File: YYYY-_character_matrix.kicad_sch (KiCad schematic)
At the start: 17 parts, among them U1 SN74LVC244A, U2 SM411006N/15, U3 SM411006N/15, U4 SN74LVC244A, U5 SM411006N/15, U6 SM411006N/15, U7 SM411006N/15

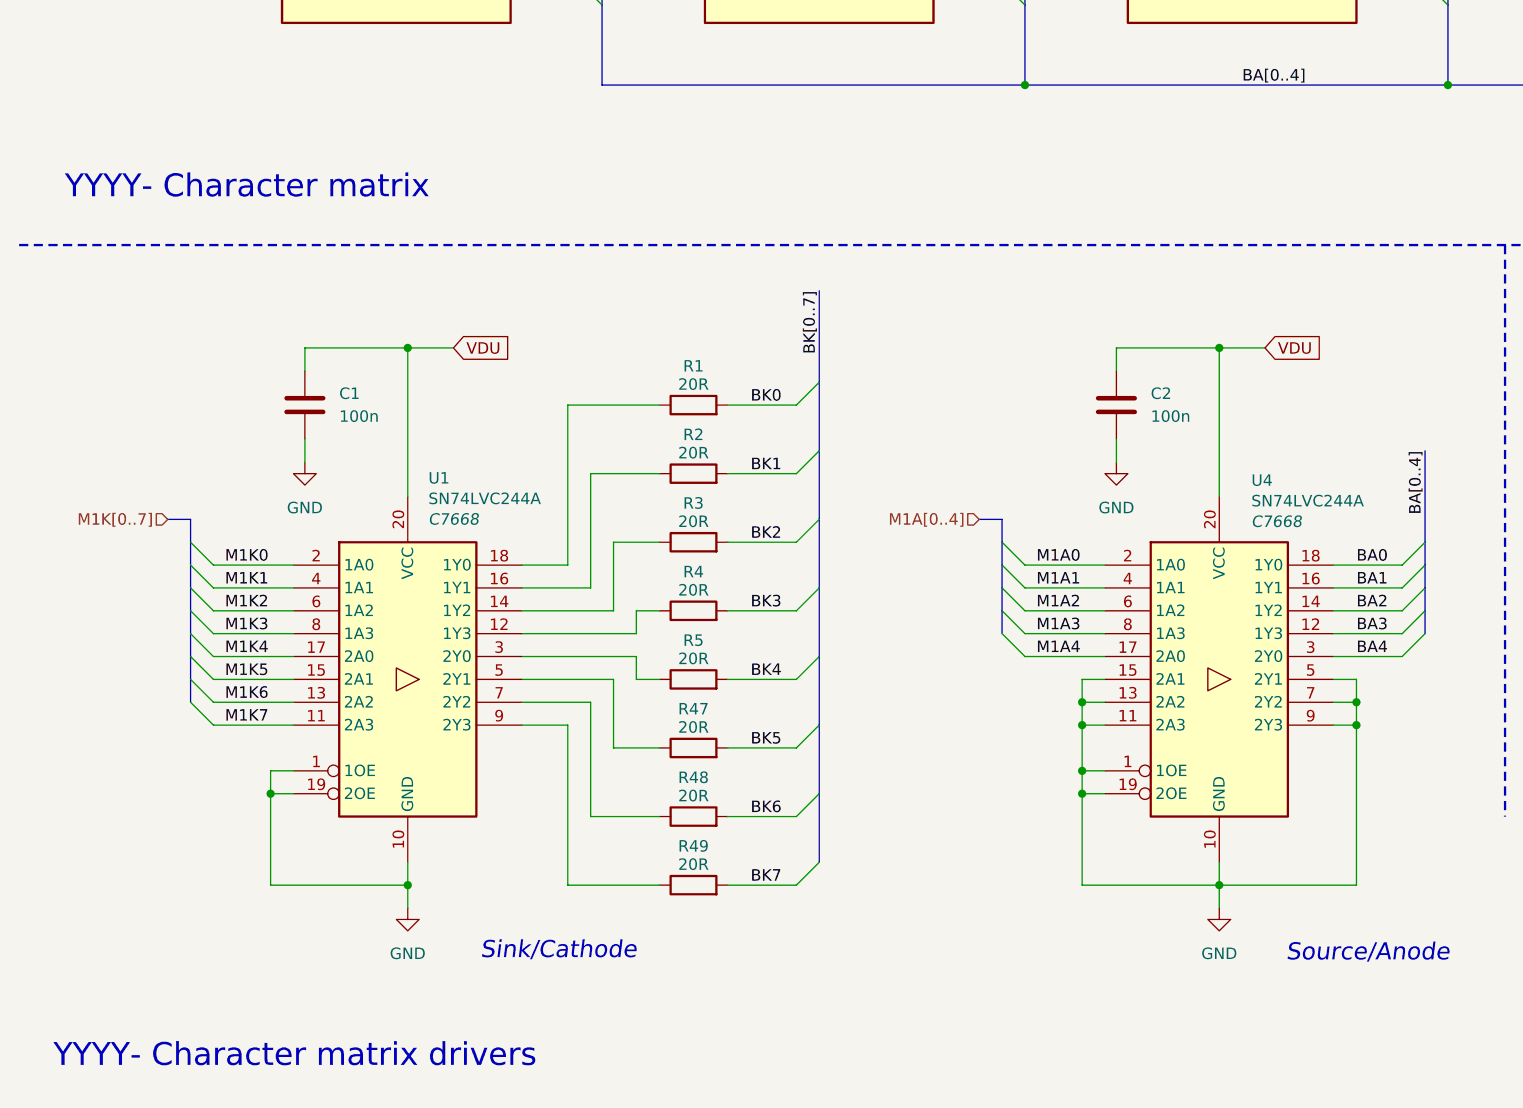
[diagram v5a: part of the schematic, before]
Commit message: verification
- sensor schematic verification
- change in the value of current limiting resistor
- disconnected unused buffer pins
- labeling or peripherals used in primary MCU
- additional user button
- DRC corrections
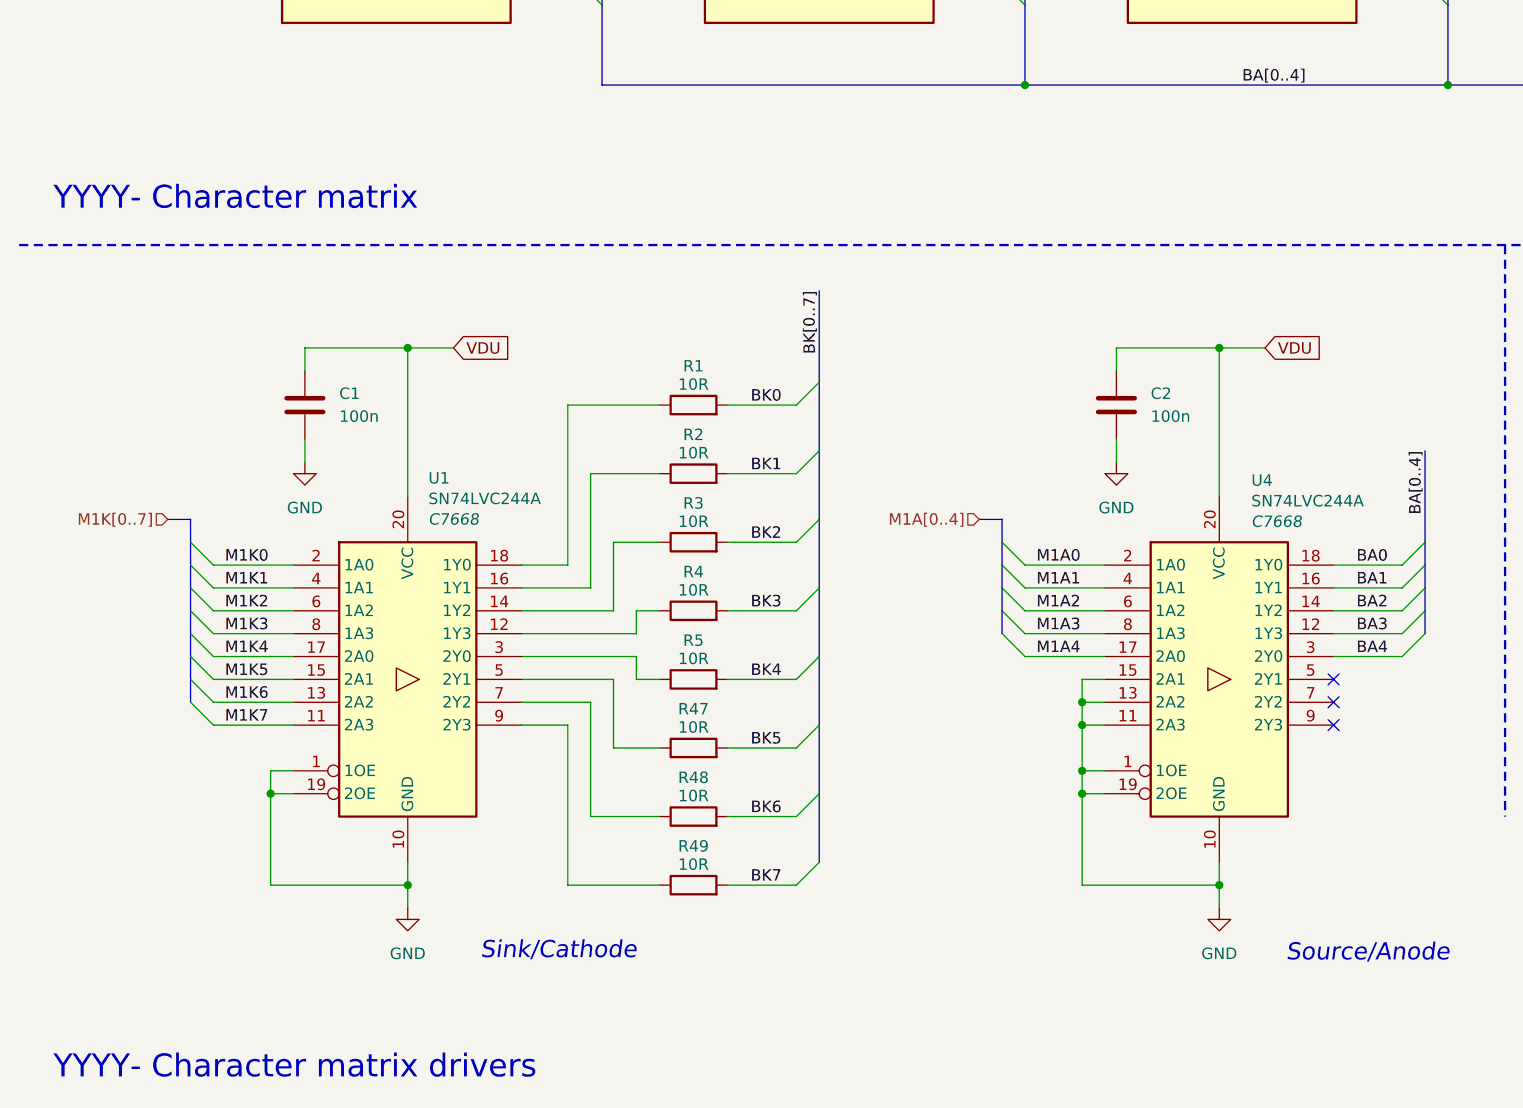
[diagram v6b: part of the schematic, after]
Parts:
- R1, R2, R3, R4, R47, R48, R49, R5: value 20R -> 10R
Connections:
- net GND: no longer U4.5 (2Y1), U4.7 (2Y2), U4.9 (2Y3)
- no-connect marks 0 -> 3
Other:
- company: Rajath Katker -> TJ71PL
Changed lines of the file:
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@@
 	(title_block
 		(title "YYYY- Character Matrix & Drivers ")
-		(date "2025-11-04")
+		(date "2025-09-05")
 		(rev "v0.0")
-		(company "Rajath Katker")
+		(company "TJ71PL")
+		(comment 1 "天計")
 		(comment 4 "Final verification pending")
 	)
@@
 	(text "YYYY- Character matrix"
 		(exclude_from_sim no)
-		(at 17.78 95.25 0)
+		(at 16.51 96.52 0)
 		(effects
 			(font
@@
 	(text "YYYY- Character matrix drivers "
 		(exclude_from_sim no)
-		(at 16.51 191.77 0)
+		(at 16.51 193.04 0)
 		(effects
 			(font
@@
 	)
 	(junction
-		(at 161.29 152.4)
-		(diameter 0)
-		(color 0 0 0 0)
-	)
-	(junction
 		(at 130.81 160.02)
 		(diameter 0)
@@
 	)
 	(junction
-		(at 161.29 154.94)
-		(diameter 0)
-		(color 0 0 0 0)
-	)
-	(junction
 		(at 78.74 31.75)
 		(diameter 0)
@@
 		(color 0 0 0 0)
 	)
+	(no_connect
+		(at 158.75 149.86)
+	)
+	(no_connect
+		(at 158.75 152.4)
+	)
+	(no_connect
+		(at 158.75 154.94)
+	)
 	(bus_entry
 		(at 31.75 142.24)
@@
 		)
 	)
-	(wire
-		(pts
-			(xy 158.75 149.86) (xy 161.29 149.86)
-		)
-		(stroke
-			(width 0)
-			(type default)
-		)
-	)
 	(bus
 		(pts
@@
 	(wire
 		(pts
-			(xy 161.29 149.86) (xy 161.29 152.4)
-		)
-		(stroke
-			(width 0)
-			(type default)
-		)
-	)
-	(wire
-		(pts
 			(xy 163.83 69.85) (xy 168.91 69.85)
 		)
@@
 		)
 	)
-	(wire
-		(pts
-			(xy 158.75 154.94) (xy 161.29 154.94)
-		)
-		(stroke
-			(width 0)
-			(type default)
-		)
-	)
 	(bus
 		(pts
@@
 	(wire
 		(pts
-			(xy 161.29 172.72) (xy 146.05 172.72)
-		)
-		(stroke
-			(width 0)
-			(type default)
-		)
-	)
-	(wire
-		(pts
 			(xy 91.44 149.86) (xy 99.06 149.86)
 		)
@@
 	(wire
 		(pts
-			(xy 161.29 154.94) (xy 161.29 172.72)
-		)
-		(stroke
-			(width 0)
-			(type default)
-		)
-	)
-	(wire
-		(pts
 			(xy 222.25 62.23) (xy 227.33 62.23)
 		)
@@
 		)
 	)
-	(wire
-		(pts
-			(xy 161.29 152.4) (xy 161.29 154.94)
-		)
-		(stroke
-			(width 0)
-			(type default)
-		)
-	)
 	(bus
 		(pts
@@
 	(wire
 		(pts
-			(xy 158.75 152.4) (xy 161.29 152.4)
-		)
-		(stroke
-			(width 0)
-			(type default)
-		)
-	)
-	(wire
-		(pts
 			(xy 146.05 172.72) (xy 146.05 175.26)
 		)
@@
 			)
 		)
-		(property "Value" "20R"
+		(property "Value" "10R"
 			(at 87.63 117.094 90)
 			(effects
@@
 			)
 		)
-		(property "Value" "20R"
+		(property "Value" "10R"
 			(at 87.63 132.334 90)
 			(effects
@@
 			)
 		)
-		(property "Value" "20R"
+		(property "Value" "10R"
 			(at 87.63 139.954 90)
 			(effects
@@
 			)
 		)
-		(property "Value" "20R"
+		(property "Value" "10R"
 			(at 87.63 155.194 90)
 			(effects
@@
 			)
 		)
-		(property "Value" "20R"
+		(property "Value" "10R"
 			(at 87.63 162.814 90)
 			(effects
@@
 			)
 		)
-		(property "Value" "20R"
+		(property "Value" "10R"
 			(at 87.63 124.714 90)
 			(effects
@@
 			)
 		)
-		(property "Value" "20R"
+		(property "Value" "10R"
 			(at 87.63 147.574 90)
 			(effects
@@
 			)
 		)
-		(property "Value" "20R"
+		(property "Value" "10R"
 			(at 87.63 170.434 90)
 			(effects

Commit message: semi final verification
- change in display type to common cathode
- verification of the schematic
- addition of footprints
- further minor changes
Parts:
- removed U2, U3, U5, U6, U7: SM411006N/15, precision_clock:SM411006N15, symbol precision_clock:SM411006N/15
- added U2, U3, U5, U6, U7: 10016AS, precision_clock:10016AS, symbol precision_clock:10016AS
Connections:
- net BA0: now also R1.2, U2.7 (A), U3.7 (A), U5.7 (A), U7.7 (A); no longer U4.18 (1Y0)
- net BA1: now also R2.2, U2.6 (B), U3.6 (B), U5.6 (B), U6.6 (B), U6.7 (A), U7.6 (B); no longer U4.16 (1Y1)
- net BA2: now also R3.2, U2.4 (C), U3.4 (C), U5.4 (C), U6.4 (C), U7.4 (C); no longer U4.14 (1Y2)
- net BA3: now also R4.2, U2.2 (D), U3.2 (D), U5.2 (D), U6.2 (D), U7.2 (D); no longer U4.12 (1Y3)
- net BA4: now also R5.2, U2.1 (E), U3.1 (E), U5.1 (E), U6.1 (E), U7.1 (E); no longer U4.3 (2Y0)
- net BK0: now also U4.18 (1Y0), U2.3 (CK), U2.8 (CK); no longer R1.2
- net BK1: now also U4.16 (1Y1), U3.3 (CK), U3.8 (CK); no longer R2.2
- net BK2: now also U4.14 (1Y2), U5.3 (CK), U5.8 (CK); no longer R3.2
- net BK3: now also U4.12 (1Y3), U6.3 (CK), U6.8 (CK); no longer R4.2
- net BK4: now also U4.3 (2Y0), U7.3 (CK), U7.8 (CK); no longer R5.2
- net M1A0: now also U1.2 (1A0); no longer U4.2 (1A0)
- net M1A1: now also U1.4 (1A1); no longer U4.4 (1A1)
- net M1A2: now also U1.6 (1A2); no longer U4.6 (1A2)
- net M1A3: now also U1.8 (1A3); no longer U4.8 (1A3)
- net M1A4: now also U1.17 (2A0); no longer U4.17 (2A0)
- net M1K0: now also U4.2 (1A0); no longer U1.2 (1A0)
- net M1K1: now also U4.4 (1A1); no longer U1.4 (1A1)
- net M1K2: now also U4.6 (1A2); no longer U1.6 (1A2)
- net M1K3: now also U4.8 (1A3); no longer U1.8 (1A3)
- net M1K4: now also U4.17 (2A0); no longer U1.17 (2A0)
- net BK5 renamed BA5
- net BA5: now also U2.9 (F), U3.9 (F), U5.9 (F), U6.9 (F), U7.9 (F)
- net BK6 renamed BA6
- net BA6: now also U2.10 (G), U3.10 (G), U5.10 (G), U6.10 (G), U7.10 (G)
- net BK7 renamed BA7
- net BA7: now also U2.5 (DP), U3.5 (DP), U5.5 (DP), U6.5 (DP), U7.5 (DP)
- net M1K5 renamed M1A5
- net M1K6 renamed M1A6
- net M1K7 renamed M1A7

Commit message: PCB routing
- JLCPCB constraints added
- removal of multiple test points
- change of footprints
- change of THT LEDs
- rough position of all the major components
- PCB routing started
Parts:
- U15: renamed from U2; footprint precision_clock:10016AS -> precision_clock:Xlitx 10016AS
- U17: renamed from U3; footprint precision_clock:10016AS -> precision_clock:Xlitx 10016AS
- U19: renamed from U5; footprint precision_clock:10016AS -> precision_clock:Xlitx 10016AS
- U20: renamed from U6; footprint precision_clock:10016AS -> precision_clock:Xlitx 10016AS
- U21: renamed from U7; footprint precision_clock:10016AS -> precision_clock:Xlitx 10016AS
- renumbered C1 to C44, C2 to C45, R1 to R33, R2 to R34, R3 to R35, R4 to R36, R5 to R37, R47 to R38, R48 to R39, R49 to R40, U1 to U16, U4 to U18
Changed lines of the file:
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@@
 		(on_board yes)
 		(dnp no)
-		(property "Reference" "R1"
+		(property "Reference" "R33"
 			(at 87.63 115.062 90)
 			(effects
@@
 			(project "Precision Clock"
 				(path "/c9a8ff63-a0d1-4125-9dd1-40fb53daf536/95a63663-b2f9-448f-a4dd-b71321e8f379"
-					(reference "R1")
+					(reference "R33")
 					(unit 1)
 				)
@@
 		(on_board yes)
 		(dnp no)
-		(property "Reference" "R3"
+		(property "Reference" "R35"
 			(at 87.63 130.302 90)
 			(effects
@@
 			(project "Precision Clock"
 				(path "/c9a8ff63-a0d1-4125-9dd1-40fb53daf536/95a63663-b2f9-448f-a4dd-b71321e8f379"
-					(reference "R3")
+					(reference "R35")
 					(unit 1)
 				)
@@
 		(dnp no)
 		(fields_autoplaced yes)
-		(property "Reference" "C2"
+		(property "Reference" "C45"
 			(at 138.43 118.1099 0)
 			(effects
@@
 			(project "Precision Clock"
 				(path "/c9a8ff63-a0d1-4125-9dd1-40fb53daf536/95a63663-b2f9-448f-a4dd-b71321e8f379"
-					(reference "C2")
+					(reference "C45")
 					(unit 1)
 				)
@@
 		(dnp no)
 		(fields_autoplaced yes)
-		(property "Reference" "#PWR04"
+		(property "Reference" "#PWR0103"
 			(at 146.05 181.61 0)
 			(effects
@@
 			(project "Precision Clock"
 				(path "/c9a8ff63-a0d1-4125-9dd1-40fb53daf536/95a63663-b2f9-448f-a4dd-b71321e8f379"
-					(reference "#PWR04")
+					(reference "#PWR0103")
 					(unit 1)
 				)
@@
 		(dnp no)
 		(fields_autoplaced yes)
-		(property "Reference" "#PWR03"
+		(property "Reference" "#PWR0102"
 			(at 134.62 132.08 0)
 			(effects
@@
 			(project "Precision Clock"
 				(path "/c9a8ff63-a0d1-4125-9dd1-40fb53daf536/95a63663-b2f9-448f-a4dd-b71321e8f379"
-					(reference "#PWR03")
+					(reference "#PWR0102")
 					(unit 1)
 				)
@@
 		(dnp no)
 		(fields_autoplaced yes)
-		(property "Reference" "U3"
+		(property "Reference" "U17"
 			(at 101.6 40.64 0)
 			(effects
@@
 			)
 		)
-		(property "Footprint" "precision_clock:10016AS"
+		(property "Footprint" "precision_clock:Xlitx 10016AS"
 			(at 101.6 60.96 0)
 			(effects
@@
 			(project "Precision Clock"
 				(path "/c9a8ff63-a0d1-4125-9dd1-40fb53daf536/95a63663-b2f9-448f-a4dd-b71321e8f379"
-					(reference "U3")
+					(reference "U17")
 					(unit 1)
 				)
@@
 		(on_board yes)
 		(dnp no)
-		(property "Reference" "R4"
+		(property "Reference" "R36"
 			(at 87.63 137.922 90)
 			(effects
@@
 			(project "Precision Clock"
 				(path "/c9a8ff63-a0d1-4125-9dd1-40fb53daf536/95a63663-b2f9-448f-a4dd-b71321e8f379"
-					(reference "R4")
+					(reference "R36")
 					(unit 1)
 				)
@@
 		(dnp no)
 		(fields_autoplaced yes)
-		(property "Reference" "U6"
+		(property "Reference" "U20"
 			(at 195.58 40.64 0)
 			(effects
@@
 			)
 		)
-		(property "Footprint" "precision_clock:10016AS"
+		(property "Footprint" "precision_clock:Xlitx 10016AS"
 			(at 195.58 60.96 0)
 			(effects
@@
 			(project "Precision Clock"
 				(path "/c9a8ff63-a0d1-4125-9dd1-40fb53daf536/95a63663-b2f9-448f-a4dd-b71321e8f379"
-					(reference "U6")
+					(reference "U20")
 					(unit 1)
 				)
@@
 		(on_board yes)
 		(dnp no)
-		(property "Reference" "U4"
+		(property "Reference" "U18"
 			(at 149.606 127.762 0)
 			(effects
@@
 			(project "Precision Clock"
 				(path "/c9a8ff63-a0d1-4125-9dd1-40fb53daf536/95a63663-b2f9-448f-a4dd-b71321e8f379"
-					(reference "U4")
+					(reference "U18")
 					(unit 1)
 				)
@@
 		(dnp no)
 		(fields_autoplaced yes)
-		(property "Reference" "#PWR01"
+		(property "Reference" "#PWR0100"
 			(at 44.45 132.08 0)
 			(effects
@@
 			(project "Precision Clock"
 				(path "/c9a8ff63-a0d1-4125-9dd1-40fb53daf536/95a63663-b2f9-448f-a4dd-b71321e8f379"
-					(reference "#PWR01")
+					(reference "#PWR0100")
 					(unit 1)
 				)
@@
 		(dnp no)
 		(fields_autoplaced yes)
-		(property "Reference" "U2"
+		(property "Reference" "U15"
 			(at 54.61 40.64 0)
 			(effects
@@
 			)
 		)
-		(property "Footprint" "precision_clock:10016AS"
+		(property "Footprint" "precision_clock:Xlitx 10016AS"
 			(at 54.61 60.96 0)
 			(effects
@@
 			(project ""
 				(path "/c9a8ff63-a0d1-4125-9dd1-40fb53daf536/95a63663-b2f9-448f-a4dd-b71321e8f379"
-					(reference "U2")
+					(reference "U15")
 					(unit 1)
 				)
@@
 		(on_board yes)
 		(dnp no)
-		(property "Reference" "R47"
+		(property "Reference" "R38"
 			(at 87.63 153.162 90)
 			(effects
@@
 			(project "Precision Clock"
 				(path "/c9a8ff63-a0d1-4125-9dd1-40fb53daf536/95a63663-b2f9-448f-a4dd-b71321e8f379"
-					(reference "R47")
+					(reference "R38")
 					(unit 1)
 				)
@@
 		(dnp no)
 		(fields_autoplaced yes)
-		(property "Reference" "C1"
+		(property "Reference" "C44"
 			(at 48.26 118.1099 0)
 			(effects
@@
 			(project "Precision Clock"
 				(path "/c9a8ff63-a0d1-4125-9dd1-40fb53daf536/95a63663-b2f9-448f-a4dd-b71321e8f379"
-					(reference "C1")
+					(reference "C44")
 					(unit 1)
 				)
@@
 		(dnp no)
 		(fields_autoplaced yes)
-		(property "Reference" "U7"
+		(property "Reference" "U21"
 			(at 242.57 40.64 0)
 			(effects
@@
 			)
 		)
-		(property "Footprint" "precision_clock:10016AS"
+		(property "Footprint" "precision_clock:Xlitx 10016AS"
 			(at 242.57 60.96 0)
 			(effects
@@
 			(project "Precision Clock"
 				(path "/c9a8ff63-a0d1-4125-9dd1-40fb53daf536/95a63663-b2f9-448f-a4dd-b71321e8f379"
-					(reference "U7")
+					(reference "U21")
 					(unit 1)
 				)
@@
 		(on_board yes)
 		(dnp no)
-		(property "Reference" "R48"
+		(property "Reference" "R39"
 			(at 87.63 160.782 90)
 			(effects
@@
 			(project "Precision Clock"
 				(path "/c9a8ff63-a0d1-4125-9dd1-40fb53daf536/95a63663-b2f9-448f-a4dd-b71321e8f379"
-					(reference "R48")
+					(reference "R39")
 					(unit 1)
 				)
@@
 		(dnp no)
 		(fields_autoplaced yes)
-		(property "Reference" "U5"
+		(property "Reference" "U19"
 			(at 148.59 40.64 0)
 			(effects
@@
 			)
 		)
-		(property "Footprint" "precision_clock:10016AS"
+		(property "Footprint" "precision_clock:Xlitx 10016AS"
 			(at 148.59 60.96 0)
 			(effects
@@
 			(project "Precision Clock"
 				(path "/c9a8ff63-a0d1-4125-9dd1-40fb53daf536/95a63663-b2f9-448f-a4dd-b71321e8f379"
-					(reference "U5")
+					(reference "U19")
 					(unit 1)
 				)
@@
 		(on_board yes)
 		(dnp no)
-		(property "Reference" "U1"
+		(property "Reference" "U16"
 			(at 58.166 127.508 0)
 			(effects
@@
 			(project "Precision Clock"
 				(path "/c9a8ff63-a0d1-4125-9dd1-40fb53daf536/95a63663-b2f9-448f-a4dd-b71321e8f379"
-					(reference "U1")
+					(reference "U16")
 					(unit 1)
 				)
@@
 		(on_board yes)
 		(dnp no)
-		(property "Reference" "R2"
+		(property "Reference" "R34"
 			(at 87.63 122.682 90)
 			(effects
@@
 			(project "Precision Clock"
 				(path "/c9a8ff63-a0d1-4125-9dd1-40fb53daf536/95a63663-b2f9-448f-a4dd-b71321e8f379"
-					(reference "R2")
+					(reference "R34")
 					(unit 1)
 				)
@@
 		(on_board yes)
 		(dnp no)
-		(property "Reference" "R5"
+		(property "Reference" "R37"
 			(at 87.63 145.542 90)
 			(effects
@@
 			(project "Precision Clock"
 				(path "/c9a8ff63-a0d1-4125-9dd1-40fb53daf536/95a63663-b2f9-448f-a4dd-b71321e8f379"
-					(reference "R5")
+					(reference "R37")
 					(unit 1)
 				)
@@
 		(on_board yes)
 		(dnp no)
-		(property "Reference" "R49"
+		(property "Reference" "R40"
 			(at 87.63 168.402 90)
 			(effects
@@
 			(project "Precision Clock"
 				(path "/c9a8ff63-a0d1-4125-9dd1-40fb53daf536/95a63663-b2f9-448f-a4dd-b71321e8f379"
-					(reference "R49")
+					(reference "R40")
 					(unit 1)
 				)
@@
 		(dnp no)
 		(fields_autoplaced yes)
-		(property "Reference" "#PWR02"
+		(property "Reference" "#PWR0101"
 			(at 55.88 181.61 0)
 			(effects
@@
 			(project "Precision Clock"
 				(path "/c9a8ff63-a0d1-4125-9dd1-40fb53daf536/95a63663-b2f9-448f-a4dd-b71321e8f379"
-					(reference "#PWR02")
-					(unit 1)
-				)
+					(reference "#PWR0101")
+					(unit 1)
+				)
